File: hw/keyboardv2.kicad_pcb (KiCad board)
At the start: 2 copper layers, 145 x 45 mm, 40 parts, among them K1 CONN_4, K2 CONN_4, K3 CONN_4, K4 CONN_4, K5 CONN_4, K6 CONN_4, K7 CONN_4, K8 CONN_4, Q1 MOSFET_N, U1 TINYMEGA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

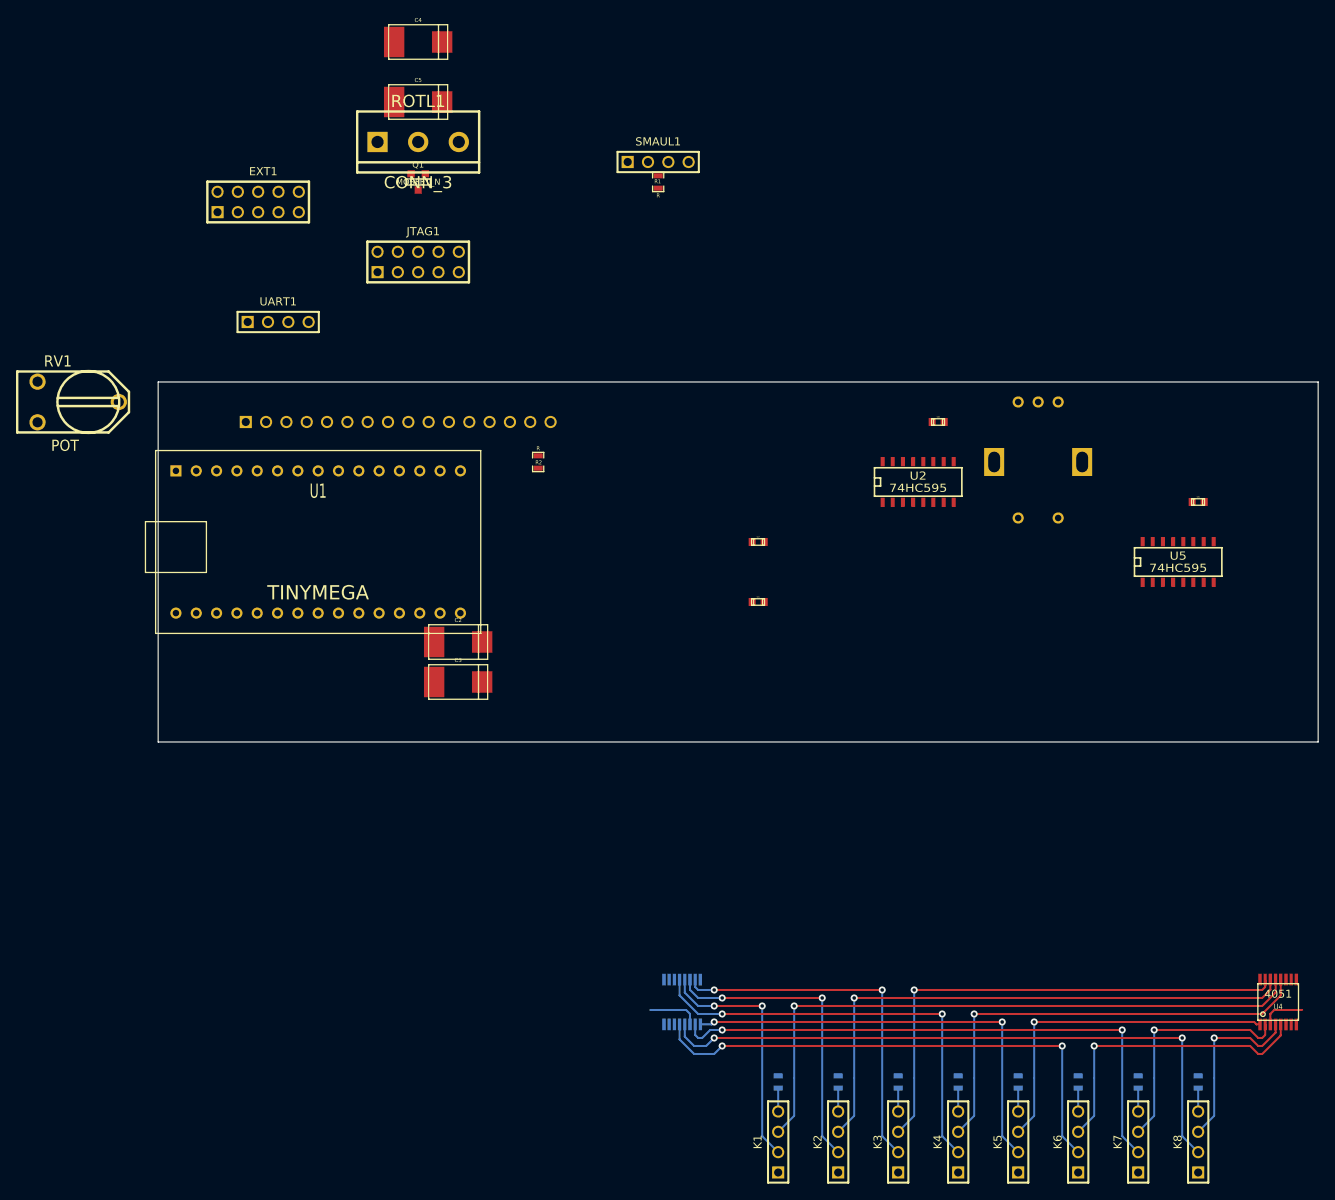
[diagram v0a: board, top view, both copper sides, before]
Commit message: Change LED pin order, complete routing of key jacks
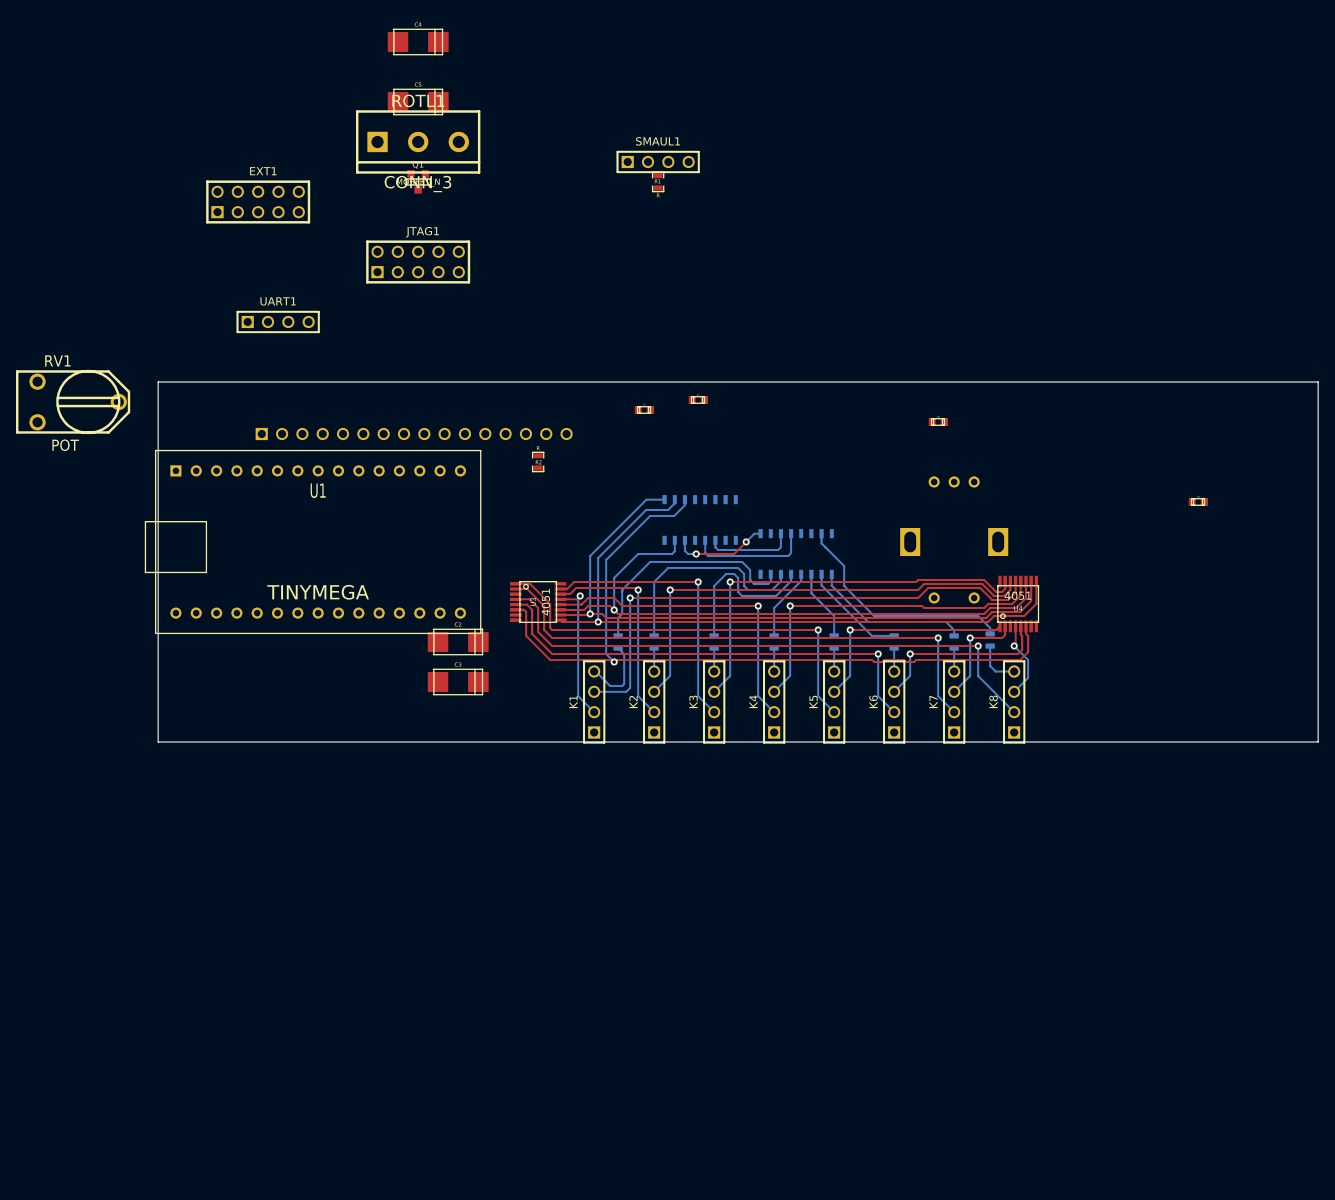
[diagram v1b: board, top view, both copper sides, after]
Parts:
- C2, C3, C4, C5: footprint c_tant_D -> c_tant_C
- EXT1, JTAG1: footprint PIN_ARRAY_5x2 -> PIN_ARRAY_5x2_BPAD
- K1, K2, K3, K4, K5, K6, K7, K8, SMAUL1, UART1: footprint PIN_ARRAY_4x1 -> PIN_ARRAY_4x1_BPAD
- LCD1: footprint pin_array_16x1 -> pin_array_16x1_BPAD
- U2, U5: moved to B.Cu
- U3: moved to F.Cu
- moved R10 61.1 mm to (184.0, 132.2)
- moved K1 59.6 mm to (134.5, 140.0)
- moved K2 59.6 mm to (142.0, 140.0)
- moved K3 59.6 mm to (149.5, 140.0)
- moved K4 59.6 mm to (157.0, 140.0)
- moved K5 59.6 mm to (164.5, 140.0)
- moved K6 59.6 mm to (172.0, 140.0)
- moved K7 59.6 mm to (179.5, 140.0)
- moved K8 59.6 mm to (187.0, 140.0)
- moved R4 59.6 mm to (142.0, 132.5)
- moved R5 59.6 mm to (149.5, 132.5)
- moved R6 59.6 mm to (157.0, 132.5)
- moved R7 59.6 mm to (164.5, 132.5)
- moved R8 59.6 mm to (172.0, 132.5)
- moved R9 59.6 mm to (179.5, 132.5)
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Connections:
- U5 pad 1: /Key Jacks/led1 -> /Key Jacks/led6
- U5 pad 15: /Key Jacks/led0 -> /Key Jacks/led7
- U5 pad 2: /Key Jacks/led2 -> /Key Jacks/led5
- U5 pad 3: /Key Jacks/led3 -> /Key Jacks/led4
- U5 pad 4: /Key Jacks/led4 -> /Key Jacks/led3
- U5 pad 5: /Key Jacks/led5 -> /Key Jacks/led2
- U5 pad 6: /Key Jacks/led6 -> /Key Jacks/led1
- U5 pad 7: /Key Jacks/led7 -> /Key Jacks/led0
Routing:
- net /Key Jacks/!KEY_EN: track 0.00 -> 99.3 mm, vias 0 -> 1
- net /Key Jacks/KEY_SEL2: track 0.00 -> 84.2 mm, vias 0 -> 1
- net /Key Jacks/KEY_SEL1: track 0.00 -> 81.9 mm, vias 0 -> 1
- net /Key Jacks/KEY_SEL0: track 0.00 -> 76.0 mm, vias 0 -> 1
- net /Key Jacks/led0: track 0.00 -> 29.1 mm
- net /Key Jacks/led7: track 0.00 -> 29.0 mm
- net /Key Jacks/led1: track 0.00 -> 26.6 mm
- net /Key Jacks/led2: track 0.00 -> 20.3 mm
- net /Key Jacks/led6: track 0.00 -> 19.8 mm
- net /Key Jacks/scio6: track 29.3 -> 13.2 mm
- net /Key Jacks/scio4: track 42.9 -> 27.5 mm
- net /Key Jacks/LED_LATCH: track 0.00 -> 15.1 mm
- net /Key Jacks/scio5: track 37.6 -> 22.8 mm
- net /Key Jacks/pwr3: track 53.9 -> 39.6 mm, vias 2 -> 1
- net /Key Jacks/scio3: track 56.8 -> 42.9 mm
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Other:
- net class Default: clearance 0.254 -> 0.249; trace_width 0.254 -> 0.25
- rule trace_clearance: 0.254 -> 0.249
- rule trace_min: 0.254 -> 0.25

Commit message: Routed all signals, only VDD/GND remaining
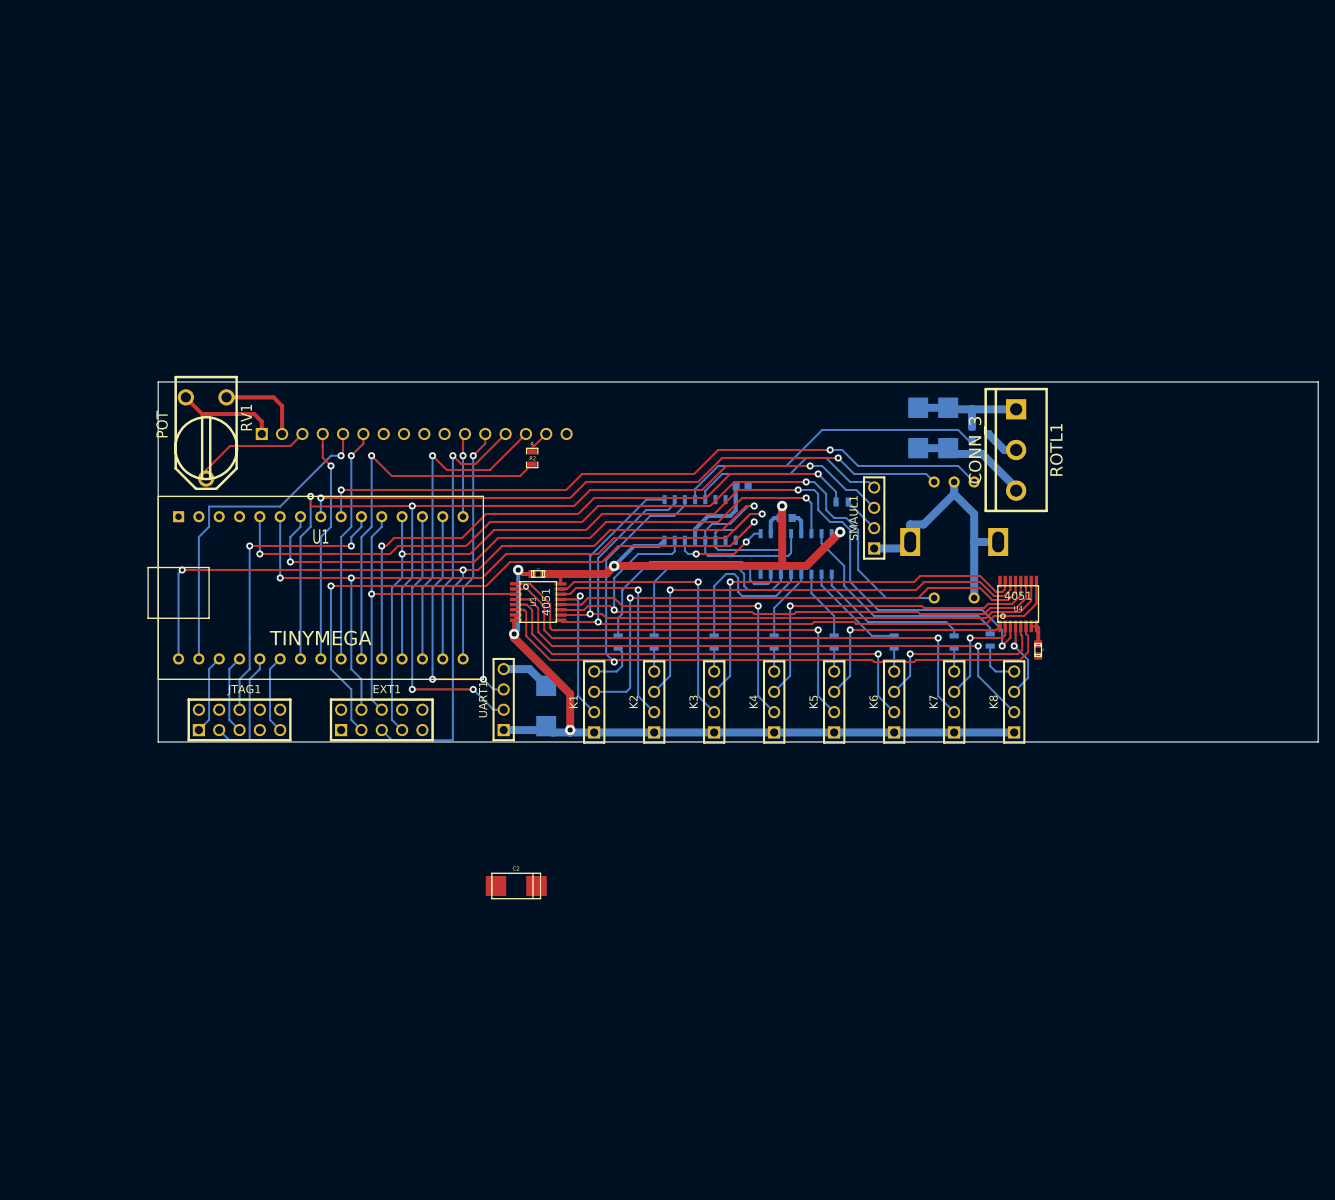
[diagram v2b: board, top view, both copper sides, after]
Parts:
- C1, C3, C4, C5, C8, Q1, R1: moved to B.Cu
- moved ROTL1 84.1 mm to (187.2, 108.5), turned to 270 degrees
- moved C4 79.0 mm to (175.0, 105.8), turned to 270 degrees
- moved C5 77.8 mm to (178.8, 105.8), turned to 270 degrees
- moved Q1 77.0 mm to (182.8, 106.5), turned to 270 degrees
- moved EXT1 66.6 mm to (108.0, 142.2)
- moved JTAG1 61.4 mm to (90.2, 142.2)
- moved UART1 55.0 mm to (123.2, 139.7), turned to 90 degrees
- moved SMAUL1 52.1 mm to (169.5, 117.0), turned to 90 degrees
- moved R1 46.1 mm to (165.5, 115.0), turned to 0 degrees
- moved C2 31.3 mm to (124.8, 163.0)
- moved C6 27.2 mm to (190.0, 133.5), turned to 270 degrees
- moved C7 24.4 mm to (127.5, 124.0)
- moved C8 22.5 mm to (158.5, 117.0), turned to 180 degrees
- moved RV1 16.6 mm to (86.0, 107.0), turned to 270 degrees
- moved C1 12.1 mm to (153.0, 113.0)
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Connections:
- net N-0000043 renamed /BLPWR
- C1 pad 1: VDD -> VCC
- C2 pad 1: VDD -> VCC
- C3 pad 1: VDD -> VCC
- C4 pad 1: VDD -> VCC
- C5 pad 1: VDD -> VCC
- C6 pad 1: VDD -> VCC
- C7 pad 1: VDD -> VCC
- C8 pad 1: VDD -> VCC
- EXT1 pad 2: VDD -> VCC
- EXT1 pad 9: VDD -> VCC
- JTAG1 pad 4: VDD -> VCC
- LCD1 pad 2: VDD -> VCC
- ROTL1 pad 3: VDD -> VCC
- RV1 pad 1: VDD -> VCC
- U1 pad 1: VDD -> VCC
- U2 pad 10: VDD -> VCC
- U2 pad 4: /BUZZER -> /BLAULICHT
- U2 pad 5: /BLAULICHT -> /BUZZER
- U3 pad 16: VDD -> VCC
- U3 pad 8: VSS -> GND
- U4 pad 16: VDD -> VCC
- U4 pad 8: VSS -> GND
- U5 pad 10: VDD -> VCC
- UART1 pad 4: VDD -> VCC
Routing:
- net GND: track 0.00 -> 168.0 mm, vias 0 -> 3
- net /Key Jacks/LED_LATCH: track 15.1 -> 141.0 mm, vias 0 -> 3
- net /Key Jacks/KEY_SCIO: track 0.00 -> 123.2 mm, vias 0 -> 3
- net /SMAUL_BTN: track 0.00 -> 116.5 mm, vias 0 -> 3
- net /ENC_PUSH: track 0.00 -> 102.8 mm, vias 0 -> 2
- net /Key Jacks/LED_SCK: track 11.0 -> 107.0 mm, vias 0 -> 3
- net VCC: track 0.00 -> 94.8 mm, vias 0 -> 3
- net /ENC_B: track 0.00 -> 86.2 mm, vias 0 -> 2
- net /ENC_A: track 0.00 -> 82.3 mm, vias 0 -> 2
- net /SOUT: track 0.00 -> 79.5 mm, vias 0 -> 2
- net /Key Jacks/LED_SIN: track 0.00 -> 78.7 mm, vias 0 -> 2
- net /SMAUL_LED: track 0.00 -> 77.1 mm, vias 0 -> 2
- net /LCD_LED: track 0.00 -> 47.7 mm, vias 0 -> 1
- net /Key Jacks/KEY_PWR: track 0.00 -> 43.2 mm, vias 0 -> 1
- net /LCD_RW: track 0.00 -> 41.5 mm, vias 0 -> 1
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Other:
- net class Default: clearance 0.249 -> 0.2
- net class Power added: clearance 0.2, trace_width 0.5, via_dia 1.3, via_drill 0.8
- rule trace_clearance: 0.249 -> 0.2

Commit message: All connections routed! \o/
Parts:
- C2, C6: moved to B.Cu
- moved C2 68.6 mm to (85.5, 106.8), turned to 180 degrees
- moved C1 13.6 mm to (141.2, 119.8), turned to 270 degrees
- moved C6 7.16 mm to (187.0, 127.0), turned to 90 degrees
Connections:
- RV1 pad 1: VCC -> GND
- RV1 pad 3: GND -> VCC
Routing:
- net GND: track 168.0 -> 491.5 mm, vias 3 -> 13
- net VCC: track 94.8 -> 350.7 mm, vias 3 -> 11
- net /BLAULICHT: track 39.6 -> 43.5 mm
- net /Key Jacks/KEY_SEL1: track 81.9 -> 84.6 mm
- net /Key Jacks/!KEY_EN: track 99.3 -> 102.1 mm
- net /Key Jacks/KEY_SEL2: track 84.6 -> 87.3 mm
- net /SOUT: track 79.5 -> 77.0 mm
- net /Key Jacks/LED_LATCH: track 141.0 -> 138.6 mm
- net /Key Jacks/LED_SCK: track 107.0 -> 108.9 mm
- net /ENC_B: track 86.2 -> 87.9 mm
- net /LCD_RW: track 41.5 -> 40.2 mm
- net /LCD_D2: track 34.5 -> 35.5 mm
- net /M_TX: track 30.3 -> 29.4 mm
- net N-0000042: track 15.0 -> 14.3 mm
- net /ENC_A: track 82.3 -> 82.9 mm
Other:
- net class Default: via_dia 0.889 -> 1.1

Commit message: Yeah, so I had the board reversed -.-   Once more with feeling.
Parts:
- C2: moved to F.Cu
- K1, K2, K3, K4, K5, K6, K7, K8, SMAUL1, UART1: footprint PIN_ARRAY_4x1_BPAD -> PIN_ARRAY_4x1_KEYED_BPAD
- moved C2 126.7 mm to (212.2, 106.3), turned to 90 degrees
- moved JTAG1 119.5 mm to (209.6, 141.9), turned to 180 degrees
- moved U1 99.4 mm to (199.8, 124.8), turned to 180 degrees
- moved LCD1 95.0 mm to (207.0, 106.5), turned to 180 degrees
- moved EXT1 83.9 mm to (191.8, 141.9), turned to 180 degrees
- moved C6 76.3 mm to (111.0, 120.0), turned to 180 degrees
- moved K8 75.0 mm to (112.0, 139.0)
- moved ROTL1 74.8 mm to (112.5, 109.0), turned to 90 degrees
- moved RV1 73.8 mm to (159.8, 106.5), turned to 0 degrees
- moved R10 69.8 mm to (114.2, 132.8)
- moved Q1 65.3 mm to (117.5, 109.0), turned to 90 degrees
- moved K7 60.0 mm to (119.5, 139.0)
- moved R9 60.0 mm to (119.5, 132.2)
- moved S1 59.0 mm to (120.5, 120.0)
- moved C5 57.5 mm to (121.2, 106.2), turned to 90 degrees
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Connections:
- RV1 pad 1: GND -> VCC
- RV1 pad 3: VCC -> GND
- U5 pad 1: /Key Jacks/led6 -> /Key Jacks/led1
- U5 pad 15: /Key Jacks/led7 -> /Key Jacks/led0
- U5 pad 2: /Key Jacks/led5 -> /Key Jacks/led2
- U5 pad 3: /Key Jacks/led4 -> /Key Jacks/led3
- U5 pad 4: /Key Jacks/led3 -> /Key Jacks/led4
- U5 pad 5: /Key Jacks/led2 -> /Key Jacks/led5
- U5 pad 6: /Key Jacks/led1 -> /Key Jacks/led6
- U5 pad 7: /Key Jacks/led0 -> /Key Jacks/led7
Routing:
- net GND: track 491.5 -> 206.7 mm, vias 13 -> 2
- net VCC: track 350.7 -> 154.5 mm, vias 11 -> 6
- net /Key Jacks/KEY_SCIO: track 123.2 -> 47.2 mm, vias 3 -> 0
- net /Key Jacks/KEY_PWR: track 43.2 -> 118.1 mm, vias 1 -> 2
- net /Key Jacks/scio7: track 9.69 -> 68.9 mm
- net /Key Jacks/pwr7: track 72.1 -> 13.3 mm
- net /Key Jacks/scio0: track 67.0 -> 12.6 mm
- net /Key Jacks/pwr6: track 67.2 -> 19.0 mm
- net /LCD_LED: track 47.7 -> 0.00 mm, vias 1 -> 0
- net /Key Jacks/pwr0: track 18.1 -> 65.7 mm
- net /Key Jacks/scio6: track 13.2 -> 60.4 mm
- net /LCD_RW: track 40.2 -> 0.00 mm, vias 1 -> 0
- net /LCD_D3: track 40.2 -> 0.00 mm, vias 1 -> 0
- net /Key Jacks/scio1: track 58.6 -> 19.0 mm
- net /!RESET: track 37.9 -> 0.00 mm, vias 2 -> 0
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
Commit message: Board complete. Again.
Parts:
- added MARKER: VAL**, MARKER, F.Cu at (130.0, 106.5)
- added MARKER: VAL**, MARKER, F.Cu at (217.2, 142.0)
- added SHACK: VAL**, SHACK, F.Cu at (145.2, 105.8)
- moved C3 1.91 mm to (169.1, 139.0)
- moved UART1 1.91 mm to (173.1, 139.0)
- moved EXT1 1.05 mm to (190.8, 141.8), turned to 0 degrees
- moved JTAG1 1.05 mm to (208.6, 141.8), turned to 0 degrees
- moved U1 0.10 mm to (199.7, 124.7)
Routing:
- net GND: track 206.7 -> 387.4 mm, vias 2 -> 9
- net VCC: track 154.5 -> 295.1 mm, vias 6 -> 11
- net /!RESET: track 0.00 -> 49.4 mm
- net /TDI: track 0.00 -> 39.7 mm
- net /TCK: track 0.00 -> 39.6 mm
- net /LCD_LED: track 0.00 -> 30.1 mm, vias 0 -> 1
- net /TDO: track 0.00 -> 28.9 mm
- net /TMS: track 0.00 -> 28.9 mm
- net /LCD_D0: track 0.00 -> 28.2 mm, vias 0 -> 1
- net /Key Jacks/LED_LATCH: track 104.9 -> 130.5 mm, vias 1 -> 3
- net /LCD_RW: track 0.00 -> 23.8 mm, vias 0 -> 1
- net /LCD_D3: track 0.00 -> 23.3 mm, vias 0 -> 1
- net /SMAUL_LED: track 91.3 -> 68.8 mm, vias 1 -> 2
- net /Key Jacks/LED_SCK: track 104.7 -> 126.7 mm, vias 1 -> 3
- net /LCD_D2: track 0.00 -> 18.1 mm, vias 0 -> 1
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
